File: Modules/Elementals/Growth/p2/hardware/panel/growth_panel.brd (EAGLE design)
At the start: 20 x 128.5 mm, 0 parts

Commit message: Rename eagle files
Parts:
- added U$1: (no value), SonicAthame:PANEL_4U
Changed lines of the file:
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@@
 <setting verticaltext="up"/>
 </settings>
-<grid distance="50" unitdist="mil" unit="mil" style="lines" multiple="1" display="yes" altdistance="10" altunitdist="mil" altunit="mil"/>
+<grid distance="50" unitdist="mil" unit="mil" style="lines" multiple="1" display="yes" altdistance="5" altunitdist="mil" altunit="mil"/>
 <layers>
 <layer number="1" name="Top" color="4" fill="1" visible="yes" active="yes"/>
@@
 <fusionsync huburn="a.cGVyc29uYWw6dWUyZGY0M2Ex" projecturn="a.cGVyc29uYWw6dWUyZGY0M2ExIzIwMjAwODA5MzIyMjM2MzA2" f3durn="urn:adsk.wipprod:dm.lineage:YbMO2u0XRLqBhb2bUnu0HA" pcbguid="2a1b8c86-2fc1-4c7e-a4a6-f594d6aae771" lastpulledtime="" lastsyncedchangeguid="52ca49c6-1b85-65ce-afc4-29855cab59a0"/>
 <plain>
-<wire x1="0" y1="0" x2="20" y2="0" width="0" layer="20"/>
-<wire x1="20" y1="0" x2="20" y2="128.5" width="0" layer="20"/>
-<wire x1="20" y1="128.5" x2="0" y2="128.5" width="0" layer="20"/>
-<wire x1="0" y1="128.5" x2="0" y2="0" width="0" layer="20"/>
 <text x="10.16" y="119.38" size="1.6764" layer="25" align="bottom-center">Sonic Athame™</text>
 <text x="10.16" y="113.665" size="1.27" layer="25" align="center">Elemental Growth</text>
@@
 <hole x="5.08" y="43.18" drill="6.3"/>
 <hole x="15.24" y="43.18" drill="6.3"/>
-<hole x="7.5" y="3" drill="3.2"/>
-<hole x="7.5" y="125.5" drill="3.2"/>
 <hole x="10.16" y="22.86" drill="7.5"/>
 <hole x="10.16" y="73.66" drill="7.5"/>
@@
 </autorouter>
 <elements>
+<element name="U$1" library="SonicAthame" library_urn="urn:adsk.eagle:library:22327399" package="PANEL_4U" package3d_urn="urn:adsk.eagle:package:26352447/2" value="" x="0" y="0" smashed="yes"/>
 </elements>
 <signals>
@@
 </drawing>
 <compatibility>
+<note version="8.2" severity="warning">
+Since Version 8.2, EAGLE supports online libraries. The ids
+of those online libraries will not be understood (or retained)
+with this version.
+</note>
 <note version="8.3" severity="warning">
 Since Version 8.3, EAGLE supports Fusion synchronisation.
@@
 the document will break the link to the Fusion PCB feature.
 </note>
+<note version="8.3" severity="warning">
+Since Version 8.3, EAGLE supports URNs for individual library
+assets (packages, symbols, and devices). The URNs of those assets
+will not be understood (or retained) with this version.
+</note>
+<note version="8.3" severity="warning">
+Since Version 8.3, EAGLE supports the association of 3D packages
+with devices in libraries, schematics, and board files. Those 3D
+packages will not be understood (or retained) with this version.
+</note>
 </compatibility>

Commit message: Replaced board holes/outlines with standard library component
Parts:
- added U$2, U$3, U$4, U$5: (no value), SonicAthame:WQP-PJ398SM_PANEL
- added U$6, U$7: (no value), SonicAthame:ALPHA_POT_VERTICAL_PANEL
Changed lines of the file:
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@@
 </layers>
 <board>
-<fusionsync huburn="a.cGVyc29uYWw6dWUyZGY0M2Ex" projecturn="a.cGVyc29uYWw6dWUyZGY0M2ExIzIwMjAwODA5MzIyMjM2MzA2" f3durn="urn:adsk.wipprod:dm.lineage:YbMO2u0XRLqBhb2bUnu0HA" pcbguid="2a1b8c86-2fc1-4c7e-a4a6-f594d6aae771" lastpulledtime="" lastsyncedchangeguid="52ca49c6-1b85-65ce-afc4-29855cab59a0"/>
+<fusionsync huburn="a.cGVyc29uYWw6dWUyZGY0M2Ex" projecturn="a.cGVyc29uYWw6dWUyZGY0M2ExIzIwMjAwODA5MzIyMjM2MzA2" f3durn="urn:adsk.wipprod:dm.lineage:HKurPCoHT-6uQ3M1nE7qNw" pcbguid="1525c07d-22f4-49ff-9dd1-695bbb3f1316" lastpulledtime="" lastsyncedchangeguid="efb5e469-ab0f-66e1-d9e4-b34b7dd1f068"/>
 <plain>
 <text x="10.16" y="119.38" size="1.6764" layer="25" align="bottom-center">Sonic Athame™</text>
@@
 <text x="10.16" y="118.745" size="1.016" layer="25" align="top-center">The Point of Modular</text>
 <text x="10.16" y="112.395" size="0.6096" layer="25" align="center">Prototype 2</text>
-<hole x="5.08" y="93.98" drill="6.3"/>
-<hole x="15.24" y="93.98" drill="6.3"/>
-<hole x="5.08" y="43.18" drill="6.3"/>
-<hole x="15.24" y="43.18" drill="6.3"/>
-<hole x="10.16" y="22.86" drill="7.5"/>
-<hole x="10.16" y="73.66" drill="7.5"/>
 <text x="5.08" y="47.117" size="1.778" layer="25" align="bottom-center">In</text>
 <text x="15.24" y="47.117" size="1.778" layer="25" align="bottom-center">Out</text>
@@
 </autorouter>
 <elements>
-<element name="U$1" library="SonicAthame" library_urn="urn:adsk.eagle:library:22327399" package="PANEL_4U" package3d_urn="urn:adsk.eagle:package:26352447/2" value="" x="0" y="0" smashed="yes"/>
+<element name="U$1" library="SonicAthame" library_urn="urn:adsk.eagle:library:22327399" package="PANEL_4U" package3d_urn="urn:adsk.eagle:package:26352447/4" value="" x="0" y="0" smashed="yes"/>
+<element name="U$2" library="SonicAthame" library_urn="urn:adsk.eagle:library:22327399" package="WQP-PJ398SM_PANEL" package3d_urn="urn:adsk.eagle:package:26352774/1" value="" x="5.08" y="93.98" smashed="yes"/>
+<element name="U$3" library="SonicAthame" library_urn="urn:adsk.eagle:library:22327399" package="WQP-PJ398SM_PANEL" package3d_urn="urn:adsk.eagle:package:26352774/1" value="" x="15.24" y="93.98" smashed="yes"/>
+<element name="U$4" library="SonicAthame" library_urn="urn:adsk.eagle:library:22327399" package="WQP-PJ398SM_PANEL" package3d_urn="urn:adsk.eagle:package:26352774/1" value="" x="5.08" y="43.18" smashed="yes"/>
+<element name="U$5" library="SonicAthame" library_urn="urn:adsk.eagle:library:22327399" package="WQP-PJ398SM_PANEL" package3d_urn="urn:adsk.eagle:package:26352774/1" value="" x="15.24" y="43.18" smashed="yes"/>
+<element name="U$6" library="SonicAthame" library_urn="urn:adsk.eagle:library:22327399" package="ALPHA_POT_VERTICAL_PANEL" package3d_urn="urn:adsk.eagle:package:26352773/1" value="" x="10.16" y="73.66" smashed="yes"/>
+<element name="U$7" library="SonicAthame" library_urn="urn:adsk.eagle:library:22327399" package="ALPHA_POT_VERTICAL_PANEL" package3d_urn="urn:adsk.eagle:package:26352773/1" value="" x="10.16" y="22.86" smashed="yes"/>
 </elements>
 <signals>

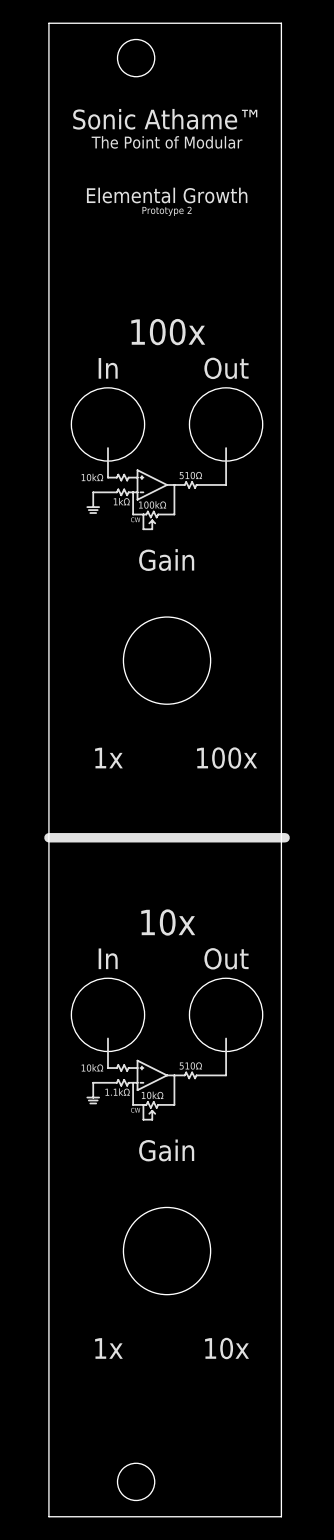
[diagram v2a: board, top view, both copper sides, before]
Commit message: Added logo to growth panel
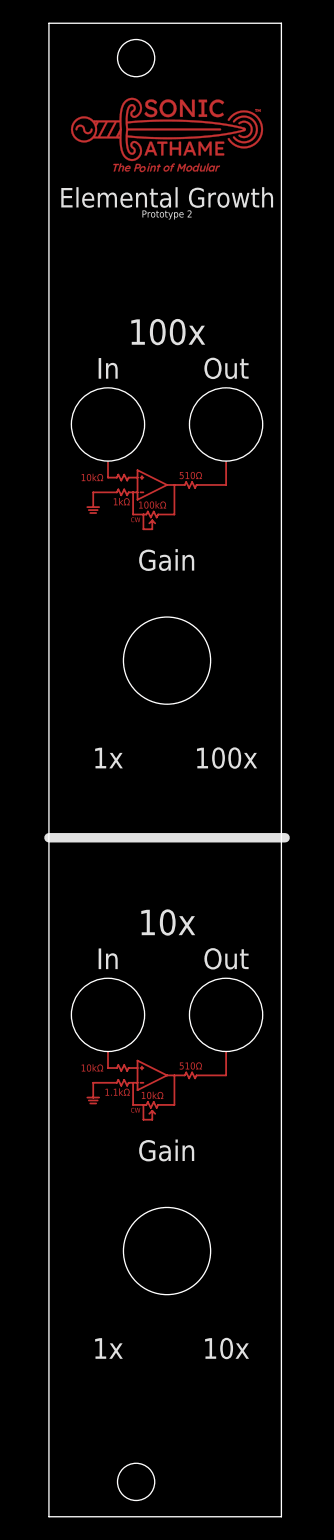
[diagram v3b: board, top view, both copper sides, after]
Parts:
- added U$8: (no value), SonicAthame:LOGO-65MIL-TPAD
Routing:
- net N$204: track 0.00 -> 3.18 mm
- net N$154: track 0.00 -> 3.17 mm
- net N$111: track 0.00 -> 2.84 mm
- net N$167: track 0.00 -> 2.84 mm
- net N$166: track 0.00 -> 2.84 mm
- net N$115: track 0.00 -> 2.84 mm
- net N$160: track 0.00 -> 2.54 mm
- net N$203: track 0.00 -> 2.54 mm
- net N$153: track 0.00 -> 2.54 mm
- net N$205: track 0.00 -> 2.54 mm
- net N$155: track 0.00 -> 2.54 mm
- net N$107: track 0.00 -> 2.54 mm
- net N$211: track 0.00 -> 2.03 mm
- net N$158: track 0.00 -> 2.03 mm
- net N$188: track 0.00 -> 1.91 mm
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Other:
- board text removed: "Sonic Athame™"
- board text removed: "The Point of Modular"

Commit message: Reposition
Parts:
- moved U$2 1.91 mm to (5.08, 92.1)
- moved U$3 1.91 mm to (15.2, 92.1)
- moved U$4 1.91 mm to (5.08, 41.3)
- moved U$5 1.91 mm to (15.2, 41.3)
- moved U$6 1.91 mm to (10.2, 71.8)
- moved U$7 1.91 mm to (10.2, 21.0)
